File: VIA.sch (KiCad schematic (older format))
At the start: 21 parts, among them J2 PORTA, J3 PORTB, J4 SD_CARD, J5 PORTD, J6 PORTC, Q1 Q_PNP_BCE, Q2 Q_NPN_BCE, U10 WD65C22, U11 WD65C22

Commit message: MAJOR FIXES - UNTESTED
Fixes for voltage regulator and barrel jack footprint. Fix for 245 direction. Fix for 65C22 PLCC pin layout. Complete rerouting of board.
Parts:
- U10, U11: symbol 6502:WD65C22 -> 6502:W65C22SxPL
- renumbered D5 to D4, D4 to D5, J4 to J2, J2 to J4, J6 to J5, J5 to J6, R6 to R7, R4 to R8, R5 to R9
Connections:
- net +5V: now also U10.21 (VDD), U11.21 (VDD); no longer U10.20 (VCC), U11.20 (VCC)
- net A3: now also U10.42 (RS0), U11.42 (RS0); no longer U10.38 (RS0), U11.38 (RS0)
- net A4: now also U10.41 (RS1), U11.41 (RS1); no longer U10.37 (RS1), U11.37 (RS1)
- net A5: now also U10.40 (RS2), U11.40 (RS2); no longer U10.36 (RS2), U11.36 (RS2)
- net A6: now also U10.39 (RS3), U11.39 (RS3); no longer U10.35 (RS3), U11.35 (RS3)
- net A7: now also U10.26 (CS1); no longer U10.24 (CS1)
- net A8: now also U11.26 (CS1); no longer U11.24 (CS1)
- net D0: now also U10.36 (D0), U11.36 (D0); no longer U10.33 (D0), U11.33 (D0)
- net D1: now also U10.35 (D1), U11.35 (D1); no longer U10.32 (D1), U11.32 (D1)
- net D2: now also U10.34 (D2), U11.34 (D2); no longer U10.31 (D2), U11.31 (D2)
- net D3: now also U10.32 (D3), U11.32 (D3); no longer U10.30 (D3), U11.30 (D3)
- net D4: now also U10.31 (D4), U11.31 (D4); no longer U10.29 (D4), U11.29 (D4)
- net D5: now also U10.30 (D5), U11.30 (D5); no longer U10.28 (D5), U11.28 (D5)
- net D6: now also U10.29 (D6), U11.29 (D6); no longer U10.27 (D6), U11.27 (D6)
- net D7: now also U10.28 (D7), U11.28 (D7); no longer U10.26 (D7), U11.26 (D7)
- net PB1: now also U10.12 (PB1); no longer U10.11 (PB1)
- net PB2: now also U10.13 (PB2); no longer U10.12 (PB2)
- net PB3: now also U10.14 (PB3); no longer U10.13 (PB3)
- net PB4: now also U10.15 (PB4); no longer U10.14 (PB4)
- net PB5: now also U10.16 (PB5); no longer U10.15 (PB5)
- net PB6: now also U10.17 (PB6); no longer U10.16 (PB6)
- net PB7: now also U10.18 (PB7); no longer U10.17 (PB7)
- net PD1: now also U11.12 (PB1); no longer U11.11 (PB1)
- net PD2: now also U11.13 (PB2); no longer U11.12 (PB2)
- net PD3: now also U11.14 (PB3); no longer U11.13 (PB3)
- net PD4: now also U11.15 (PB4); no longer U11.14 (PB4)
- net PD5: now also U11.16 (PB5); no longer U11.15 (PB5)
- net PD6: now also U11.17 (PB6); no longer U11.16 (PB6)
- net PD7: now also U11.18 (PB7); no longer U11.17 (PB7)
- net PH2: now also U10.27 (ϕ2), U11.27 (ϕ2); no longer U10.25 (PHI2), U11.25 (PHI2)
- net RW_RAW: now also U10.24 (R/~W), U11.24 (R/~W); no longer U10.22 (R/~W), U11.22 (R/~W)
- net ~IOCE: now also U10.25 (~CS2), U11.25 (~CS2); no longer U10.23 (~CS2), U11.23 (~CS2)
- net ~RESET: now also U10.37 (~RES), U11.37 (~RES); no longer U10.34 (~RESET), U11.34 (~RESET)
- net at J3.9 (Pin_9): now also U10.19 (CB1); no longer U10.18 (CB1)
- net at J3.11 (Pin_11): now also U10.20 (CB2); no longer U10.19 (CB2)
- net at D4.1 (K): now also U10.23 (~IRQ); no longer U10.21 (~IRQ)
- net at J6.9 (Pin_9): now also U11.19 (CB1); no longer U11.18 (CB1)
- net at J6.11 (Pin_11): now also U11.20 (CB2); no longer U11.19 (CB2)
- net at D6.1 (K): now also U11.23 (~IRQ); no longer U11.21 (~IRQ)
- net at J5.11 (Pin_11): now also U11.43 (CA2); no longer U11.39 (CA2)
- net at J5.9 (Pin_9): now also U11.44 (CA1); no longer U11.40 (CA1)
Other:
- moved on the sheet: C12, C13, C14, C15, C16, C17, D4, D5, D6, J2, J3, J4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

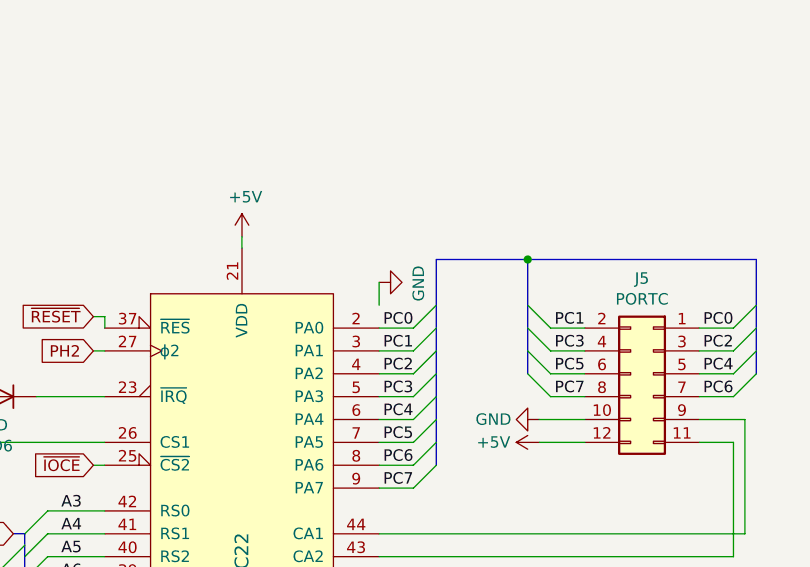
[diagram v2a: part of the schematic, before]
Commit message: Fix for bank decoder logic
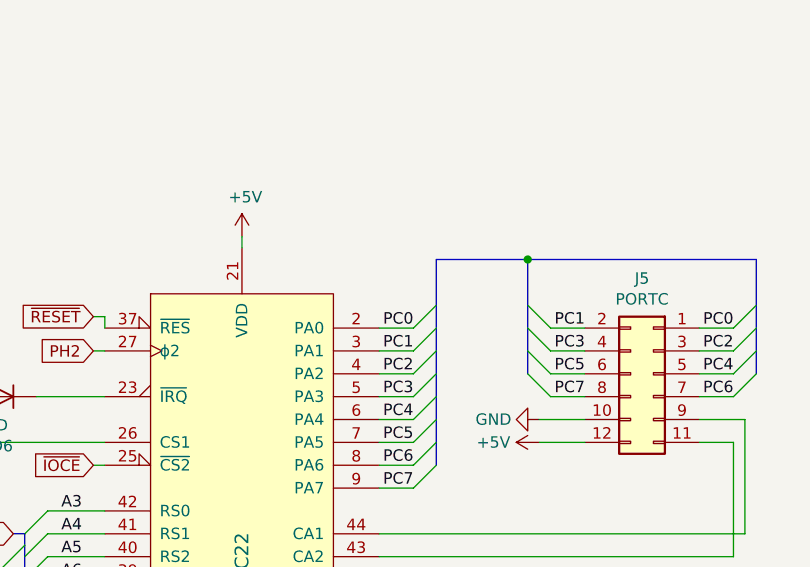
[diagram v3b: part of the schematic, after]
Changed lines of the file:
@@
 Wire Wire Line
 	4350 5400 4150 5400
-Wire Wire Line
-	8550 3350 8550 3250
 Entry Wire Line
 	8800 4050 8700 4150
@@
 Wire Wire Line
 	8550 4650 8750 4650
-$Comp
-L power:GND #PWR?
-U 1 1 5FE11CE7
-P 8550 3250
-AR Path="/5FE11CE7" Ref="#PWR?"  Part="1"
-AR Path="/5FD33D0C/5FE11CE7" Ref="#PWR?"  Part="1"
-AR Path="/60C81ED7/5FE11CE7" Ref="#PWR049"  Part="1"
-F 0 "#PWR049" H 8550 3000 50  0001 C CNN
-F 1 "GND" H 8555 3077 50  0000 C CNN
-F 2 "" H 8550 3250 50  0001 C CNN
-F 3 "" H 8550 3250 50  0001 C CNN
-	1    8550 3250
-	0    -1   1    0
-$EndComp
 Text GLabel 7300 4050 0    50   Input ~ 0
 ~IOCE
